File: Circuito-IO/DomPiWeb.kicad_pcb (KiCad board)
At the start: 2 copper layers, 90 x 55 mm, 73 parts, among them J1 Entrada 12v, J10 Bx3, J11 Bx2, J12 Bx3, J13 Salida 1, J14 Salida 2, J2 Salida 5v, J3 Serial, J4 Salida 5v Controlada, J5 EXP2, J6 RaspberryPi GPIO, J8 EXP1, J9 Bx2, K1 FINDER-36.11, K2 FINDER-36.11, Q2 DMG2305UXQ6, Q3 BC848, Q4 BC848, Q5 BC848, U1 LM2596S-ADJ

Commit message: Nueva placa
Nueva placa
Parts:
- removed C15, C16, C17, C18: 100nf, Capacitor_SMD:C_0805_2012Metric_Pad1.18x1.45mm_HandSolder
- removed C19: 470uf, Capacitor_Tantalum_SMD:CP_EIA-7343-43_Kemet-X_Pad2.25x2.55mm_HandSolder
- removed D10: Led SMD, LED_SMD:LED_1206_3216Metric_Pad1.42x1.75mm_HandSolder
- removed the J4 at (118.0, 72.0)
- removed the J5 at (176.6, 68.5)
- removed Q3, Q4, Q5: BC848, Package_TO_SOT_SMD:SOT-23
- removed R25, R26, R27, R30, R31, R32, R33, R34, R35, R36, R37, R38, R39, R40, R41, R42: 1K, Resistor_SMD:R_0805_2012Metric_Pad1.20x1.40mm_HandSolder
- removed R43, R44: 10K, Resistor_SMD:R_0805_2012Metric_Pad1.20x1.40mm_HandSolder
- added C1: 100nf, Capacitor_SMD:C_0805_2012Metric_Pad1.18x1.45mm_HandSolder, F.Cu at (150.0, 67.0)
- added C2: 100nf, Capacitor_SMD:C_0805_2012Metric_Pad1.18x1.45mm_HandSolder, F.Cu at (91.5, 82.0)
- added C3: 100nf, Capacitor_SMD:C_0805_2012Metric_Pad1.18x1.45mm_HandSolder, B.Cu at (97.5, 108.0)
- added C7: 100nf, Capacitor_SMD:C_0805_2012Metric_Pad1.18x1.45mm_HandSolder, B.Cu at (120.5, 94.0)
- added D4: PMEG4050EP, Diode_SMD:D_SOD-128, F.Cu at (125.0, 77.0)
- added D6: LL4148, Diode_SMD:D_MiniMELF, F.Cu at (158.0, 81.0)
- added F1: Fuse, Fuse:Fuseholder_Cylinder-5x20mm_Schurter_0031_8201_Horizontal_Open, F.Cu at (95.8, 78.5)
- added F2: Fuse, Fuse:Fuseholder_Cylinder-5x20mm_Schurter_0031_8201_Horizontal_Open, F.Cu at (154.8, 66.0)
- added Q1: BC848, Package_TO_SOT_SMD:SOT-23, F.Cu at (153.0, 98.0)
- added R10: 1K, Resistor_SMD:R_0805_2012Metric_Pad1.20x1.40mm_HandSolder, F.Cu at (138.0, 72.0)
- added R11: 1K, Resistor_SMD:R_0805_2012Metric_Pad1.20x1.40mm_HandSolder, F.Cu at (100.0, 94.0)
- added R12: 1K, Resistor_SMD:R_0805_2012Metric_Pad1.20x1.40mm_HandSolder, F.Cu at (102.5, 94.0)
- added R15: 1K, Resistor_SMD:R_0805_2012Metric_Pad1.20x1.40mm_HandSolder, F.Cu at (115.5, 94.0)
- added R18: 1K, Resistor_SMD:R_0805_2012Metric_Pad1.20x1.40mm_HandSolder, F.Cu at (130.0, 77.0)
- added R20: 3K3, Resistor_SMD:R_0805_2012Metric_Pad1.20x1.40mm_HandSolder, F.Cu at (133.5, 77.0)
- added R21: 22R, Resistor_SMD:R_0805_2012Metric_Pad1.20x1.40mm_HandSolder, F.Cu at (138.0, 94.0)
- added R5: 1K, Resistor_SMD:R_0805_2012Metric_Pad1.20x1.40mm_HandSolder, F.Cu at (125.5, 83.5)
- added R6: 1K, Resistor_SMD:R_0805_2012Metric_Pad1.20x1.40mm_HandSolder, F.Cu at (130.5, 83.5)
- added R7: 1K, Resistor_SMD:R_0805_2012Metric_Pad1.20x1.40mm_HandSolder, F.Cu at (120.5, 83.5)
- C4: value 100nf -> 470uf; footprint Capacitor_SMD:C_0805_2012Metric_Pad1.18x1.45mm_HandSolder -> Capacitor_Tantalum_SMD:CP_EIA-7343-43_Kemet-X_Pad2.25x2.55mm_HandSolder
- C5: value 470uf -> 100nf; footprint Capacitor_Tantalum_SMD:CP_EIA-7343-43_Kemet-X_Pad2.25x2.55mm_HandSolder -> Capacitor_SMD:C_0805_2012Metric_Pad1.18x1.45mm_HandSolder; moved to B.Cu
- C6: moved to F.Cu
- C9: value 100nf -> 470uf; footprint Capacitor_SMD:C_0805_2012Metric_Pad1.18x1.45mm_HandSolder -> Capacitor_Tantalum_SMD:CP_EIA-7343-43_Kemet-X_Pad2.25x2.55mm_HandSolder; moved to F.Cu
- D1: value LL4148 -> M7; footprint Diode_SMD:D_MiniMELF -> Diode_SMD:D_SOD-128
- D2: value LL4148 -> Led SMD; footprint Diode_SMD:D_MiniMELF -> LED_SMD:LED_1206_3216Metric_Pad1.42x1.75mm_HandSolder
- D3: value M7 -> Led SMD; footprint Diode_SMD:D_SOD-128 -> LED_SMD:LED_1206_3216Metric_Pad1.42x1.75mm_HandSolder
- D5: value PMEG4050EP -> LL4148; footprint Diode_SMD:D_SOD-128 -> Diode_SMD:D_MiniMELF
- Q2: value DMG2305UXQ6 -> BC848
- R1, R13, R14, R4, R9: value 22R -> 1K
- R16, R17: value 10K -> 1K
- R22: value 1K -> 22R
- R23, R24: value 1K -> 10K
- R3: value 3K3 -> 1K
- moved D1 70.6 mm to (91.5, 75.0)
- moved D3 63.9 mm to (148.0, 115.0), turned to 90 degrees
- moved C9 55.0 mm to (116.0, 65.5), turned to 180 degrees
- moved D5 46.6 mm to (158.0, 98.0), turned to 90 degrees
- moved J8 40.8 mm to (147.5, 107.5), turned to 90 degrees
- moved C4 40.7 mm to (116.0, 70.5), turned to 180 degrees
- moved U1 40.3 mm to (120.2, 68.0)
- moved R22 36.0 mm to (141.0, 94.0), turned to -90 degrees
- moved R9 34.4 mm to (138.0, 68.5), turned to 180 degrees
- moved L1 34.4 mm to (128.9, 68.0)
- moved R13 33.0 mm to (105.0, 94.0), turned to 90 degrees
- moved R3 31.5 mm to (133.0, 83.5), turned to -90 degrees
- moved C12 30.8 mm to (105.0, 94.0)
- moved C11 30.8 mm to (110.0, 94.0)
- moved R14 30.5 mm to (110.0, 94.0), turned to 90 degrees
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- renumbered J13 to J10, J14 to J11, J8 to J2, J9 to J3, J10 to J4, J11 to J5, J12 to J6, J6 to J7, J3 to J8, J2 to J9
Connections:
- C4 pad 1: +5VD -> Net-(C2-Pad1)
- C5 pad 1: +5VD -> Net-(C5-Pad1)
- C6 pad 1: Net-(C6-Pad1) -> Net-(C1-Pad1)
- C8 pad 1: +5VD -> Net-(C8-Pad1)
- C9 pad 1: +5VD -> Net-(C1-Pad1)
- D1 pad 1: Net-(C18-Pad1) -> Net-(C2-Pad1)
- D2 pad 1: Net-(C18-Pad1) -> GND
- D3 pad 1: Net-(C18-Pad1) -> GND
- D5 pad 2: GND -> Net-(D5-Pad2)
- J1 pad 1: Net-(D3-Pad2) -> Net-(D1-Pad2)
- J10 pad 1: Net-(J13-Pad1) -> GND
- J10 pad 2: Net-(J13-Pad2) -> Net-(J10-Pad2)
- J11 pad 1: Net-(J14-Pad1) -> GND
- J11 pad 2: Net-(J14-Pad2) -> Net-(J11-Pad2)
- J2 pad 1: +5VD -> Net-(C1-Pad1)
- J2 pad 3: Net-(J8-Pad3) -> Net-(J2-Pad3)
- J2 pad 4: Net-(J8-Pad4) -> Net-(J2-Pad4)
- J2 pad 5: Net-(J8-Pad5) -> Net-(J2-Pad5)
- J2 pad 8: Net-(J8-Pad8) -> Net-(J2-Pad8)
- J2 pad 9: Net-(J8-Pad9) -> Net-(J2-Pad9)
- J3 pad 1: +5VD -> Net-(C3-Pad1)
- J4 pad 3: Net-(J10-Pad3) -> Net-(J4-Pad3)
- J5 pad 1: Net-(J11-Pad1) -> Net-(J5-Pad1)
- J6 pad 1: Net-(J12-Pad1) -> Net-(J6-Pad1)
- J6 pad 2: Net-(J12-Pad2) -> Net-(J6-Pad2)
- J6 pad 3: Net-(J12-Pad3) -> Net-(J6-Pad3)
- J7 pad 10: Net-(J6-Pad10) -> Net-(J7-Pad10)
- J7 pad 11: Net-(J6-Pad11) -> Net-(J7-Pad11)
- J7 pad 12: Net-(J6-Pad12) -> unconnected-(J7-Pad12)
- J7 pad 13: unconnected-(J6-Pad13) -> Net-(J7-Pad13)
- J7 pad 16: Net-(J6-Pad16) -> Net-(J7-Pad16)
- J7 pad 18: Net-(J6-Pad18) -> Net-(J7-Pad18)
- J7 pad 19: Net-(J6-Pad19) -> Net-(J7-Pad19)
- J7 pad 21: Net-(J6-Pad21) -> Net-(J7-Pad21)
- J7 pad 22: unconnected-(J6-Pad22) -> Net-(C5-Pad1)
- J7 pad 23: Net-(J6-Pad23) -> Net-(J7-Pad23)
- J7 pad 24: Net-(J6-Pad24) -> Net-(C7-Pad1)
- J7 pad 26: Net-(C10-Pad1) -> Net-(C8-Pad1)
- J7 pad 28: Net-(C16-Pad1) -> Net-(C10-Pad1)
- J7 pad 29: Net-(C12-Pad1) -> Net-(J7-Pad29)
- J7 pad 3: Net-(C15-Pad1) -> unconnected-(J7-Pad3)
- J7 pad 31: Net-(C11-Pad1) -> unconnected-(J7-Pad31)
- J7 pad 32: Net-(J6-Pad32) -> Net-(C11-Pad1)
- J7 pad 33: Net-(J6-Pad33) -> unconnected-(J7-Pad33)
- J7 pad 35: Net-(J6-Pad35) -> unconnected-(J7-Pad35)
- J7 pad 36: Net-(J6-Pad36) -> Net-(C12-Pad1)
- J7 pad 38: Net-(J6-Pad38) -> Net-(C13-Pad1)
- J7 pad 40: Net-(J6-Pad40) -> Net-(C14-Pad1)
- J7 pad 5: Net-(C14-Pad1) -> Net-(J7-Pad5)
- J7 pad 7: Net-(C13-Pad1) -> Net-(J7-Pad7)
- J7 pad 8: Net-(J6-Pad8) -> Net-(J7-Pad8)
- J8 pad 1: Net-(J3-Pad1) -> Net-(J8-Pad1)
- J8 pad 2: Net-(J3-Pad2) -> Net-(J8-Pad2)
- J9 pad 1: +5VD -> Net-(C1-Pad1)
- K1 pad 11: Net-(J13-Pad1) -> Net-(J10-Pad2)
- K1 pad 14: Net-(J13-Pad2) -> Net-(D5-Pad1)
- K1 pad A1: Net-(C18-Pad1) -> Net-(D5-Pad1)
- K1 pad A2: Net-(D1-Pad2) -> Net-(D5-Pad2)
- K2 pad 11: Net-(J14-Pad1) -> Net-(J11-Pad2)
- K2 pad 14: Net-(J14-Pad2) -> Net-(D5-Pad1)
- K2 pad A1: Net-(C18-Pad1) -> Net-(D5-Pad1)
- K2 pad A2: Net-(D2-Pad2) -> Net-(D6-Pad2)
- L1 pad 1: Net-(D5-Pad1) -> Net-(D4-Pad1)
- L1 pad 2: +5VD -> Net-(C1-Pad1)
- Q2 pad 2: +5VD -> GND
- Q2 pad 3: Net-(C6-Pad1) -> Net-(D6-Pad2)
- R1 pad 1: Net-(J6-Pad19) -> Net-(J7-Pad16)
- R1 pad 2: Net-(J5-Pad2) (its old number) -> Net-(D2-Pad2)
- R13 pad 1: Net-(J6-Pad10) -> Net-(J4-Pad3)
- R13 pad 2: Net-(J3-Pad1) -> Net-(C12-Pad1)
- R14 pad 1: Net-(J6-Pad8) -> Net-(J5-Pad1)
- R14 pad 2: Net-(J3-Pad2) -> Net-(C11-Pad1)
- R16 pad 1: GND -> Net-(J6-Pad1)
- R16 pad 2: Net-(Q3-Pad1) -> Net-(C8-Pad1)
- R17 pad 1: Net-(Q2-Pad1) -> Net-(J6-Pad2)
- R17 pad 2: +5VD -> Net-(C7-Pad1)
- R19 pad 1: Net-(Q3-Pad3) -> Net-(J6-Pad3)
- R19 pad 2: Net-(Q2-Pad1) -> Net-(C5-Pad1)
- R2 pad 1: Net-(R2-Pad1) -> Net-(J7-Pad18)
- R2 pad 2: GND -> Net-(D3-Pad2)
- R22 pad 1: Net-(J8-Pad3) -> Net-(J7-Pad8)
- R22 pad 2: Net-(J6-Pad36) -> Net-(J8-Pad2)
- R23 pad 1: Net-(J8-Pad4) -> Net-(J7-Pad5)
- R23 pad 2: Net-(J6-Pad11) -> Net-(Q1-Pad1)
- R24 pad 1: Net-(J8-Pad5) -> Net-(J7-Pad7)
- R24 pad 2: Net-(J6-Pad12) -> Net-(Q2-Pad1)
- R3 pad 1: +5VD -> Net-(J2-Pad3)
- R3 pad 2: Net-(R2-Pad1) -> Net-(J7-Pad13)
- R4 pad 1: Net-(J6-Pad32) -> Net-(J2-Pad4)
- R4 pad 2: Net-(J5-Pad3) -> Net-(J7-Pad11)
- R8 pad 1: Net-(J6-Pad23) -> Net-(J2-Pad8)
- R8 pad 2: Net-(Q5-Pad1) -> Net-(J7-Pad21)
- R9 pad 1: Net-(J6-Pad33) -> Net-(J2-Pad9)
- R9 pad 2: Net-(J5-Pad4) -> Net-(J7-Pad29)
- U1 pad 1: Net-(C18-Pad1) -> Net-(C2-Pad1)
- U1 pad 2: Net-(D5-Pad1) -> Net-(D4-Pad1)
- U1 pad 4: Net-(R2-Pad1) -> Net-(R18-Pad1)
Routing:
- net Net-(D5-Pad1): track 0.00 -> 86.4 mm
- net Net-(D1-Pad2): track 0.00 -> 75.4 mm
- net Net-(C3-Pad1): track 0.00 -> 52.1 mm
- net Net-(J11-Pad2): track 0.00 -> 38.9 mm
- net Net-(D2-Pad2): track 0.00 -> 30.9 mm
- net Net-(D3-Pad2): track 0.00 -> 27.7 mm
- net Net-(J6-Pad3): track 0.00 -> 25.0 mm
- net Net-(J6-Pad2): track 0.00 -> 24.0 mm
- net Net-(J6-Pad1): track 0.00 -> 23.0 mm
- net Net-(J5-Pad1): track 0.00 -> 22.1 mm
- net Net-(J4-Pad3): track 0.00 -> 22.1 mm
- net Net-(J5-Pad2): track 0.00 -> 21.9 mm
- net Net-(J4-Pad2): track 0.00 -> 21.1 mm
- net Net-(Q1-Pad1): track 0.00 -> 21.0 mm
- net Net-(J10-Pad2): track 0.00 -> 20.7 mm
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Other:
- board size 90 x 55 mm -> 90 x 60 mm
- board text removed: "5v"
- board text removed: "ARGENTINA"
- board text removed: "Gnd"
- board text removed: "HECHO EN"
- board text removed: "IO1"
- board text removed: "IO2"
- board text removed: "IO3"
- board text removed: "IO4"
- board text removed: "IO5"
- board text removed: "IO6"
- board text removed: "IO7"
- board text removed: "IO8"

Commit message: Placa sin pistas
Placa sin pistas
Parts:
- C4: value 470uf -> 10uf
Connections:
- J7 pad 2: unconnected-(J7-Pad2) -> Net-(C1-Pad1)
- J7 pad 4: unconnected-(J7-Pad4) -> Net-(C1-Pad1)
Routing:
- net Net-(D5-Pad1): track 86.4 -> 0.00 mm
- net Net-(D1-Pad2): track 75.4 -> 0.00 mm
- net Net-(C3-Pad1): track 52.1 -> 0.00 mm
- net Net-(J11-Pad2): track 38.9 -> 0.00 mm
- net Net-(D2-Pad2): track 30.9 -> 1.22 mm
- net Net-(D3-Pad2): track 27.7 -> 0.00 mm
- net Net-(J6-Pad3): track 25.0 -> 0.00 mm
- net Net-(J6-Pad2): track 24.0 -> 0.00 mm
- net Net-(J6-Pad1): track 23.0 -> 0.00 mm
- net Net-(J5-Pad1): track 22.1 -> 0.00 mm
- net Net-(J4-Pad3): track 22.1 -> 0.00 mm
- net Net-(J5-Pad2): track 21.9 -> 0.00 mm
- net Net-(J4-Pad2): track 21.1 -> 0.00 mm
- net Net-(Q1-Pad1): track 21.0 -> 0.00 mm
- net Net-(J10-Pad2): track 20.7 -> 0.00 mm
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
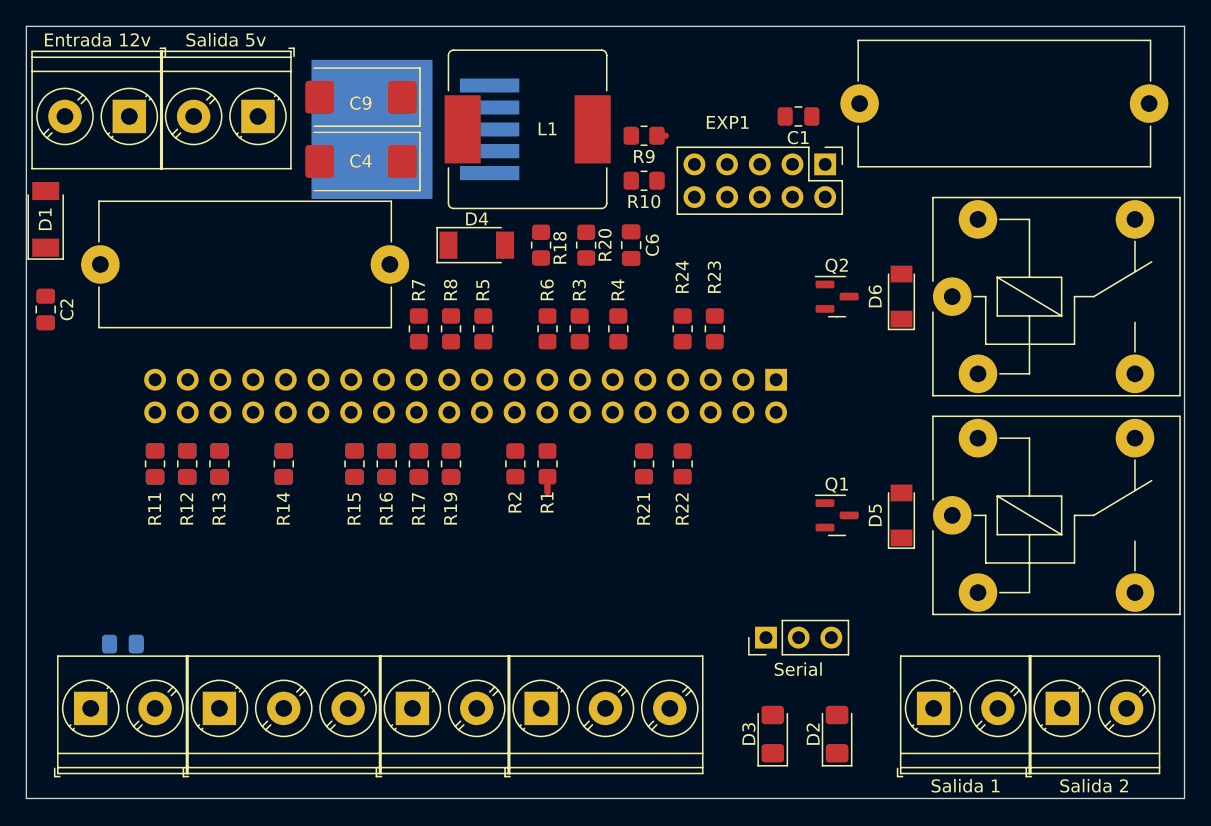
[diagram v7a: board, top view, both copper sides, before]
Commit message: PCB completo
PCB completo. Con cambios en leyendas y en el esquema para simplificar el PCB
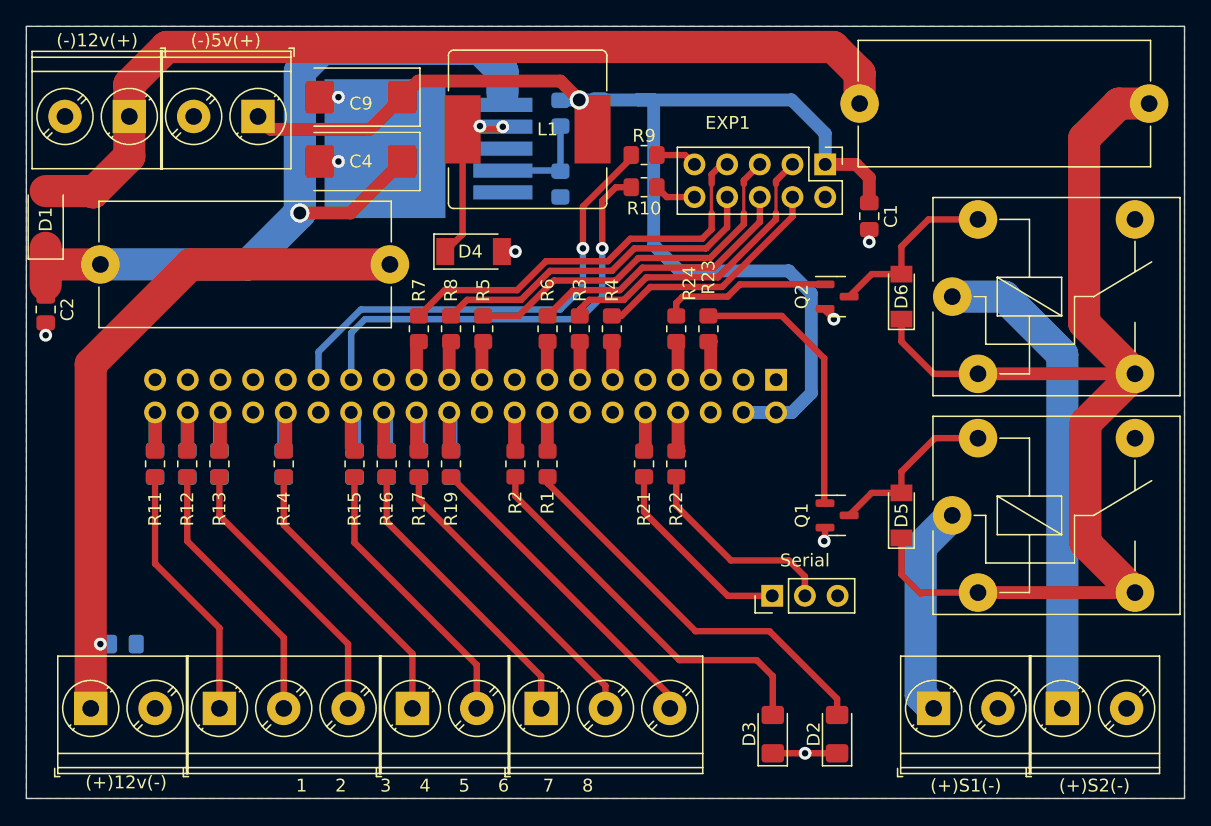
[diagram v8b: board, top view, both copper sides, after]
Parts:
- C6, R18, R20: moved to B.Cu
- J1: value Entrada 12v -> (-)12v(+)
- J10: value Salida 1 -> (+)S1(-)
- J11: value Salida 2 -> (+)S2(-)
- J3: value Bx2 -> (+)12v(-)
- J9: value Salida 5v -> (-)5v(+)
- moved C6 10.6 mm to (134.5, 66.8)
- moved R20 10.4 mm to (131.5, 66.8), turned to -90 degrees
- moved C1 9.50 mm to (155.5, 74.8), turned to -90 degrees
- moved R18 4.98 mm to (131.5, 72.2)
- moved J8 3.29 mm to (148.0, 104.2)
- moved U1 1.82 mm to (121.2, 69.5)
- moved R9 1.50 mm to (138.0, 70.0)
- moved D4 0.56 mm to (124.8, 77.5)
- moved R10 0.50 mm to (138.0, 72.5)
- moved R22 0.50 mm to (140.5, 94.0)
- moved R23 0.50 mm to (143.0, 83.5)
- moved R24 0.50 mm to (140.5, 83.5)
- moved R4 0.50 mm to (135.5, 83.5)
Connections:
- J10 pad 1: GND -> Net-(K1-Pad11)
- J10 pad 2: Net-(J10-Pad2) -> GND
- J11 pad 1: GND -> Net-(J11-Pad1)
- J11 pad 2: Net-(J11-Pad2) -> GND
- K1 pad 11: Net-(J10-Pad2) -> Net-(K1-Pad11)
- K2 pad 11: Net-(J11-Pad2) -> Net-(J11-Pad1)
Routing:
- net Net-(C1-Pad1): track 1.41 -> 97.4 mm, vias 0 -> 1
- net Net-(D5-Pad1): track 0.00 -> 88.9 mm
- net Net-(D1-Pad2): track 0.00 -> 74.5 mm
- net Net-(C2-Pad1): track 1.00 -> 65.1 mm, vias 0 -> 1
- net Net-(C3-Pad1): track 0.00 -> 53.9 mm, vias 0 -> 1
- net Net-(J11-Pad1): track 0.00 -> 37.9 mm
- net Net-(J7-Pad29): track 0.00 -> 36.6 mm, vias 0 -> 1
- net Net-(J7-Pad27): track 0.00 -> 34.4 mm, vias 0 -> 1
- net Net-(J2-Pad7): track 0.00 -> 31.3 mm
- net Net-(D3-Pad2): track 0.00 -> 30.3 mm
- net Net-(D2-Pad2): track 1.22 -> 31.2 mm
- net Net-(J2-Pad5): track 0.00 -> 28.4 mm
- net Net-(J2-Pad8): track 0.00 -> 26.7 mm
- net Net-(J6-Pad3): track 0.00 -> 25.0 mm
- net Net-(J6-Pad2): track 0.00 -> 24.0 mm
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- added copper zone on B.Cu, net GND
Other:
- board text added: "1 2 3 4 5 6 7 8"
